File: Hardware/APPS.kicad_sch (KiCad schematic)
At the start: 20 parts, among them SW1 SW_Push, U1 STM32L4P5RET6, Y1 Crystal 8 MHz

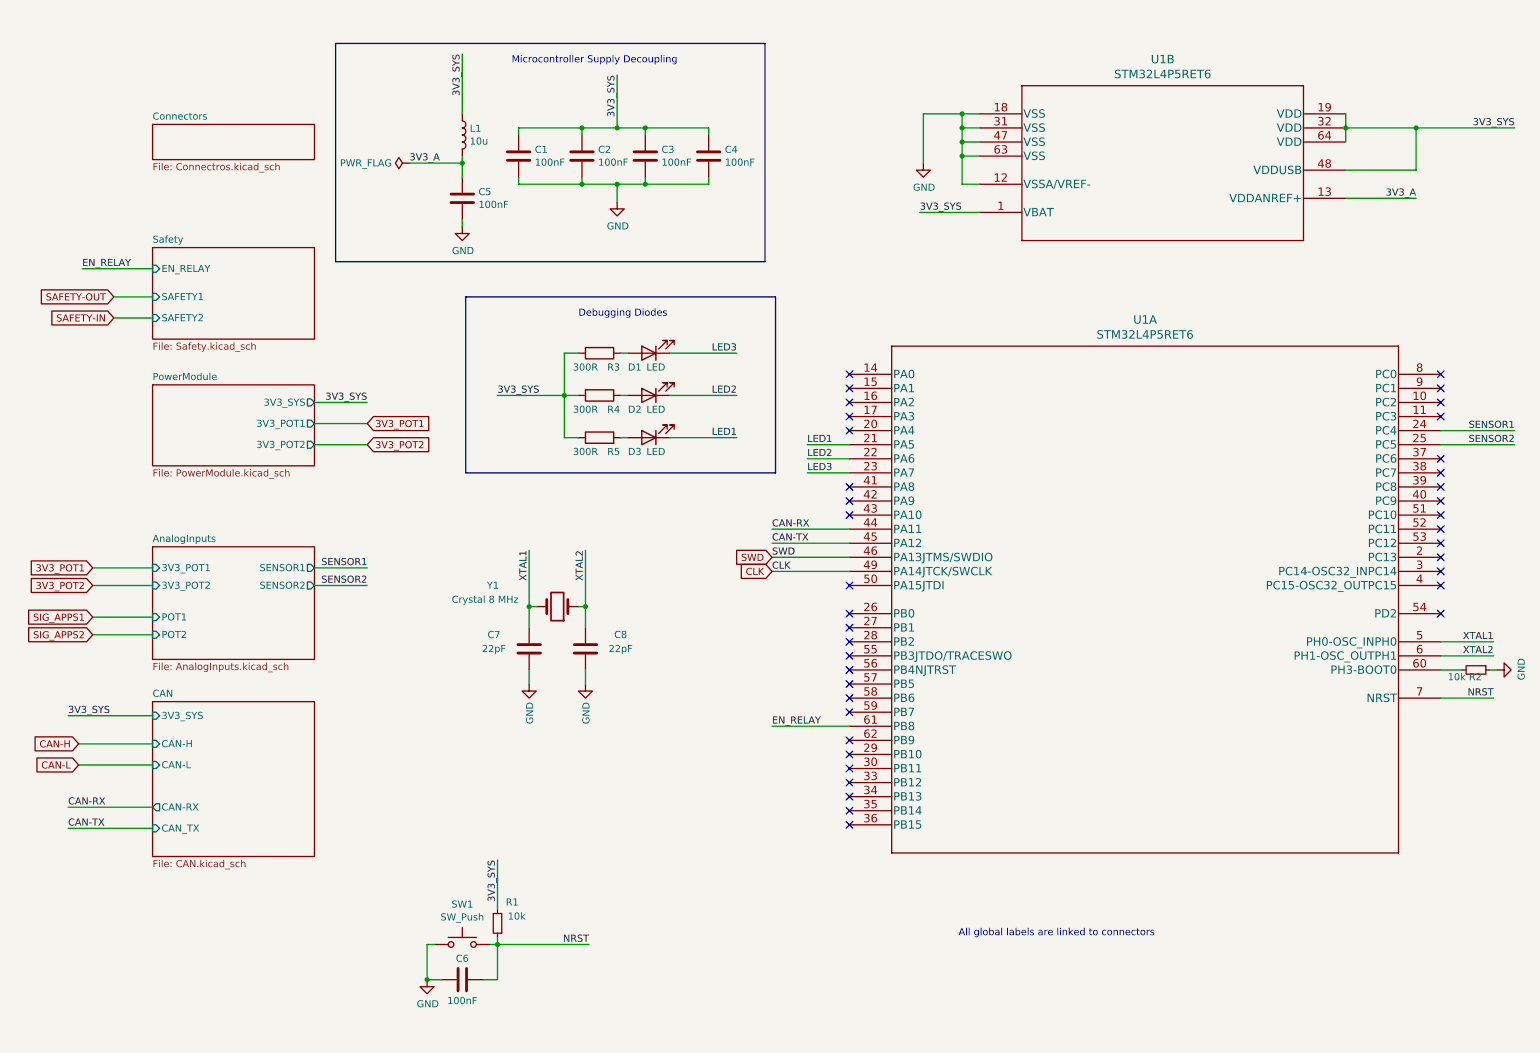
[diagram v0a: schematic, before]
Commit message: Schematic cleanup and description
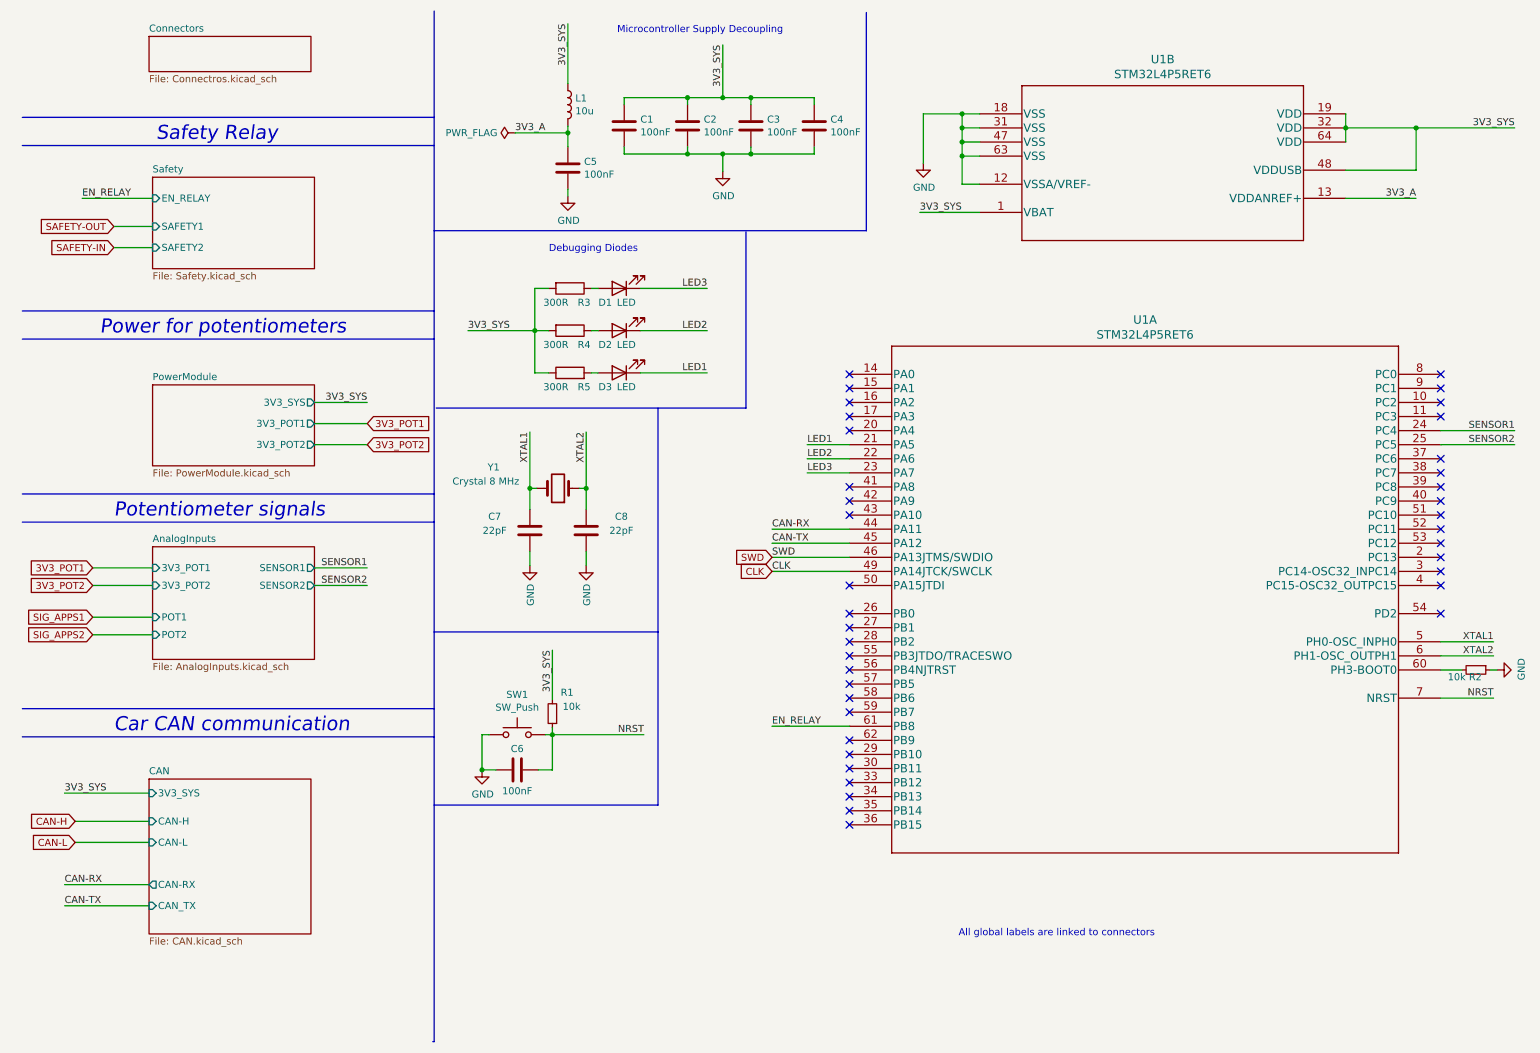
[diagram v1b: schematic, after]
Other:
- note added: "Car CAN communication"
- note added: "Potentiometer signals"
- note added: "Power for potentiometers"
- note added: "Safety Relay"
- moved on the sheet: C1, C2, C3, C4, C5, C6, C7, C8, D1, D2, D3, L1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

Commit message: PCB layout and routing
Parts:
- C5: footprint Capacitor_SMD:C_1206_3216Metric -> Capacitor_SMD:C_0603_1608Metric_Pad1.08x0.95mm_HandSolder
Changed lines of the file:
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@@
       (effects (font (size 1.27 1.27)) (justify left))
     )
-    (property "Footprint" "Capacitor_SMD:C_1206_3216Metric" (id 2) (at 111.4552 44.069 0)
+    (property "Footprint" "Capacitor_SMD:C_0603_1608Metric_Pad1.08x0.95mm_HandSolder" (id 2) (at 111.4552 44.069 0)
       (effects (font (size 1.27 1.27)) hide)
     )
@@
       (reference "#PWR0110") (unit 1) (value "GND") (footprint "")
     )
-    (path "/00000000-0000-0000-0000-00006077b773/97b42d25-e8ef-4cce-8b23-9b6436401edc"
+    (path "/00000000-0000-0000-0000-00006077b773/19768f2f-1e95-477c-97b8-06e4b42f3896"
       (reference "#PWR0111") (unit 1) (value "+24V") (footprint "")
     )
@@
     )
     (path "/00000000-0000-0000-0000-00005f621186"
-      (reference "C5") (unit 1) (value "100nF") (footprint "Capacitor_SMD:C_1206_3216Metric")
+      (reference "C5") (unit 1) (value "100nF") (footprint "Capacitor_SMD:C_0603_1608Metric_Pad1.08x0.95mm_HandSolder")
     )
     (path "/00000000-0000-0000-0000-00005f62a6cf"

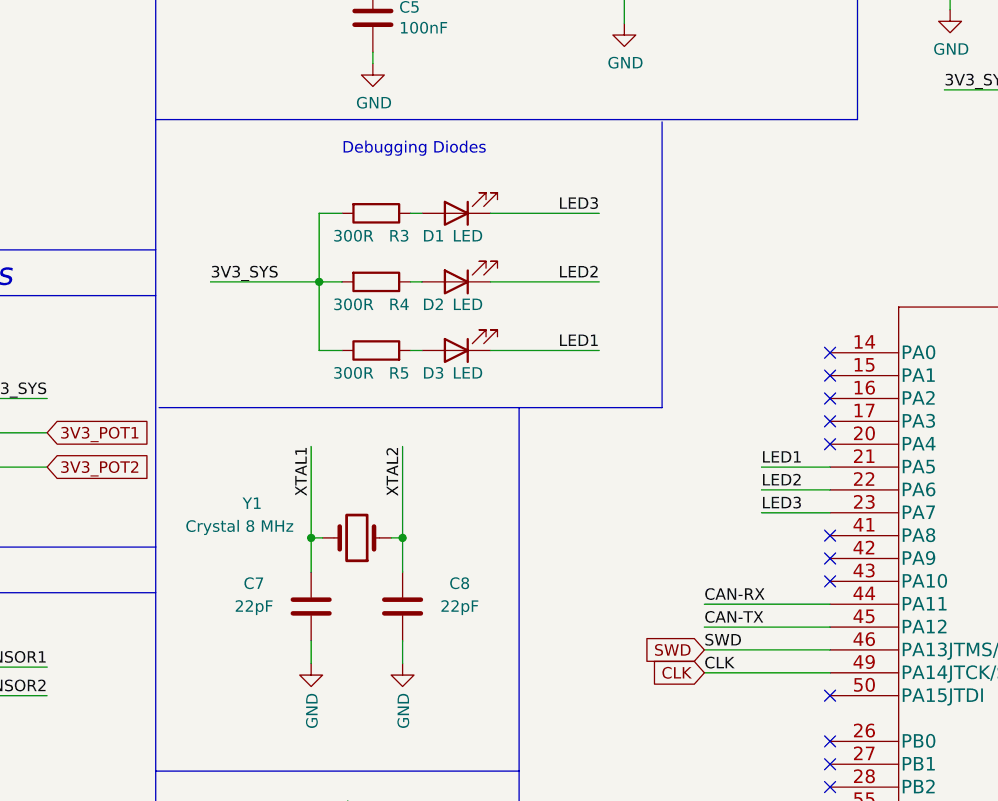
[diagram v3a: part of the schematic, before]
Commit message: Changed crystal footprint, fixed capactiors, added debug LED
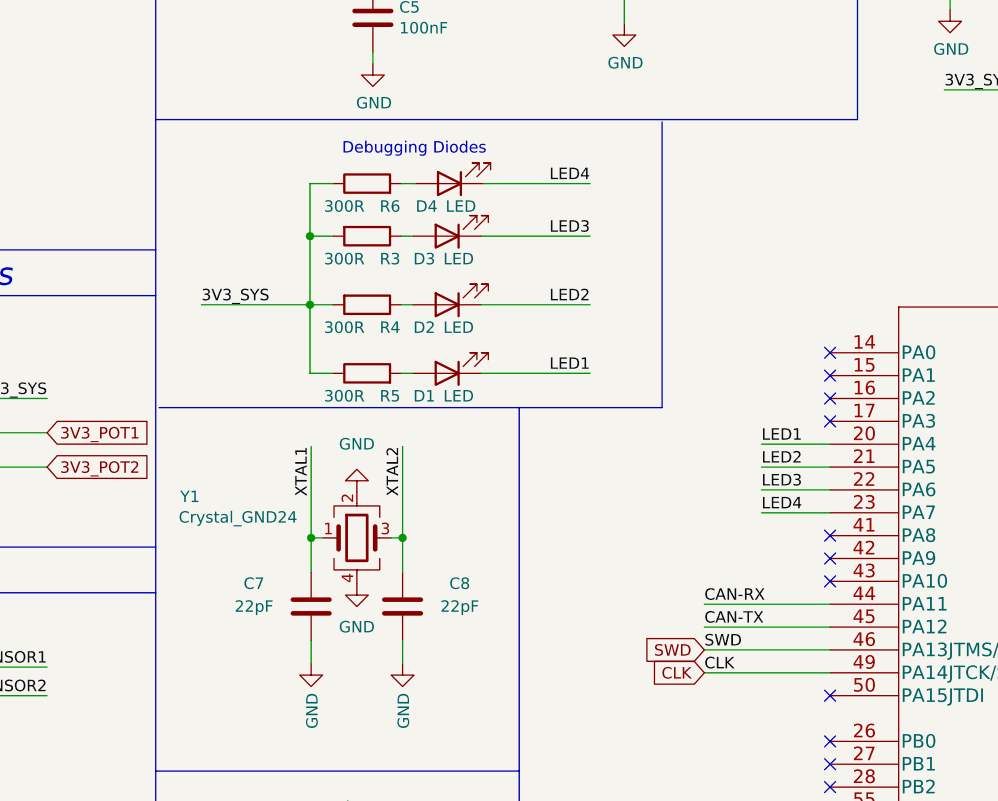
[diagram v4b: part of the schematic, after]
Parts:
- removed Y1: Crystal 8 MHz, Crystal:Crystal_SMD_HC49-SD, symbol Device:Crystal
- added D4: LED, LED_SMD:LED_0603_1608Metric_Pad1.05x0.95mm_HandSolder, symbol Device:LED
- added R6: 300R, Resistor_SMD:R_0603_1608Metric_Pad0.98x0.95mm_HandSolder, symbol Device:R
- added Y1: Crystal_GND24, Crystal:Crystal_SMD_2520-4Pin_2.5x2.0mm, symbol Device:Crystal_GND24
- U1: footprint footprints:STM32L4P5RET6 -> LQFP-64
- U1: footprint footprints:STM32L4P5RET6 -> Package_QFP:LQFP-64_10x10mm_P0.5mm
- renumbered D3 to D1, D1 to D3
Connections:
- net 3V3_SYS: now also R6.1
- net GND: now also Y1.2, Y1.4
- net LED1: now also U1.20 (PA4); no longer U1.21 (PA5)
- net LED2: now also U1.21 (PA5); no longer U1.22 (PA6)
- net LED3: now also U1.22 (PA6); no longer U1.23 (PA7)
- net XTAL1: now also Y1.1
- net XTAL2: now also Y1.3
- new net: D4.2 (A), R6.2
- new net LED4: D4.1 (K), U1.23 (PA7)
- no-connect marks 39 -> 38
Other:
- moved on the sheet: D1, D2, D3, R3, R4, R5

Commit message: Schematic cleanup
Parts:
- removed unit 2 of U1
- U1: footprint LQFP-64 -> Package_QFP:LQFP-64_10x10mm_P0.5mm; symbol 2021-05-10_08-39-16:STM32L4P5RET6 -> STM32L4P5RET6:STM32L4P5RET6
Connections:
- net 3V3_A: now also U1.13 (VDDA/VREF+)
- net 3V3_SYS: now also U1.1 (VBAT), U1.19 (VDD), U1.32 (VDD), U1.48 (VDDUSB), U1.64 (VDD)
- net GND: now also U1.12 (VSSA/VREF-), U1.18 (VSS), U1.31 (VSS), U1.47 (VSS), U1.63 (VSS)
- no-connect marks 38 -> 0
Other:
- note added: "Debug diodes"
- note added: "Oscilator"
- note added: "Reset button"
- note removed: "All global labels are linked to connectors"
- note removed: "Debugging Diodes"
- title: (none) -> PUT Motorsport EV APPS
- moved on the sheet: C1, C2, C3, C4, C5, C6, C7, C8, D1, D2, D3, D4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

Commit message: Generated BOM
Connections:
- no-connect marks 0 -> 38
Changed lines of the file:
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@@
   (junction (at 231.394 141.224) (diameter 0) (color 0 0 0 0)
   )
+  (no_connect (at 249.174 59.436))
+  (no_connect (at 249.174 56.896))
+  (no_connect (at 249.174 54.356))
+  (no_connect (at 249.174 51.816))
+  (no_connect (at 249.174 110.236))
+  (no_connect (at 249.174 112.776))
+  (no_connect (at 249.174 107.696))
+  (no_connect (at 249.174 94.996))
+  (no_connect (at 249.174 97.536))
+  (no_connect (at 249.174 100.076))
+  (no_connect (at 249.174 102.616))
+  (no_connect (at 249.174 105.156))
+  (no_connect (at 249.174 89.916))
+  (no_connect (at 249.174 77.216))
+  (no_connect (at 249.174 74.676))
+  (no_connect (at 249.174 72.136))
+  (no_connect (at 213.614 94.996))
+  (no_connect (at 213.614 92.456))
+  (no_connect (at 213.614 87.376))
+  (no_connect (at 213.614 115.316))
+  (no_connect (at 213.614 117.856))
+  (no_connect (at 213.614 100.076))
+  (no_connect (at 213.614 102.616))
+  (no_connect (at 213.614 105.156))
+  (no_connect (at 213.614 107.696))
+  (no_connect (at 249.174 125.476))
+  (no_connect (at 249.174 128.016))
+  (no_connect (at 249.174 130.556))
+  (no_connect (at 249.174 133.096))
+  (no_connect (at 249.174 122.936))
+  (no_connect (at 249.174 120.396))
+  (no_connect (at 249.174 117.856))
+  (no_connect (at 213.614 133.096))
+  (no_connect (at 213.614 130.556))
+  (no_connect (at 213.614 120.396))
+  (no_connect (at 213.614 122.936))
+  (no_connect (at 213.614 125.476))
+  (no_connect (at 213.614 128.016))
   (wire (pts (xy 263.144 79.756) (xy 249.174 79.756))
     (stroke (width 0) (type default) (color 0 0 0 0))
@@
     (stroke (width 0) (type default) (color 0 0 0 0))
   )
-  (wire (pts (xy 213.614 65.786) (xy 204.089 65.786))
+  (wire (pts (xy 199.136 65.786) (xy 213.614 65.786))
     (stroke (width 0) (type default) (color 0 0 0 0))
   )
@@
     (effects (font (size 1.27 1.27)) (justify right bottom))
   )
-  (label "NRST" (at 204.089 65.786 0)
-    (effects (font (size 1.27 1.27)) (justify left bottom))
-  )
   (label "3V3_SYS" (at 236.474 33.274 270)
     (effects (font (size 1.27 1.27)) (justify right bottom))
@@
   (label "CAN-RX" (at 19.685 169.545 0)
     (effects (font (size 1.27 1.27)) (justify left bottom))
-  )
-  (label "NRST" (at 149.098 172.212 180)
-    (effects (font (size 1.27 1.27)) (justify right bottom))
   )
   (global_label "CLK" (shape input) (at 263.144 87.376 0) (fields_autoplaced)
@@
     )
   )
+  (global_label "NRST" (shape input) (at 199.136 65.786 180) (fields_autoplaced)
+    (effects (font (size 1.27 1.27)) (justify right))
+    (property "Intersheet References" "${INTERSHEET_REFS}" (id 0) (at 192.0342 65.7066 0)
+      (effects (font (size 1.27 1.27)) (justify right) hide)
+    )
+  )
   (global_label "SAFETY-IN" (shape input) (at 28.575 54.61 180) (fields_autoplaced)
     (effects (font (size 1.27 1.27)) (justify right))
@@
     (effects (font (size 1.27 1.27)) (justify left))
     (property "Intersheet References" "${INTERSHEET_REFS}" (id 0) (at 269.3992 84.9154 0)
+      (effects (font (size 1.27 1.27)) (justify left) hide)
+    )
+  )
+  (global_label "NRST" (shape input) (at 149.098 172.212 0) (fields_autoplaced)
+    (effects (font (size 1.27 1.27)) (justify left))
+    (property "Intersheet References" "${INTERSHEET_REFS}" (id 0) (at 156.1998 172.2914 0)
       (effects (font (size 1.27 1.27)) (justify left) hide)
     )
@@
     )
     (path "/00000000-0000-0000-0000-00006077b773/ce8385db-ca62-4bf6-93c6-ac67711339c8"
-      (reference "R11") (unit 1) (value "220R") (footprint "Resistor_SMD:R_1206_3216Metric")
+      (reference "R11") (unit 1) (value "220R") (footprint "Resistor_SMD:R_0603_1608Metric_Pad0.98x0.95mm_HandSolder")
     )
     (path "/00000000-0000-0000-0000-00006068dc5c/00000000-0000-0000-0000-0000606aa78d"
@@
     )
     (path "/00000000-0000-0000-0000-00006077b773/ec62a549-ea11-4f6d-b4c1-112c7a1678a2"
-      (reference "R13") (unit 1) (value "0R") (footprint "Resistor_SMD:R_1206_3216Metric")
+      (reference "R13") (unit 1) (value "0R") (footprint "Resistor_SMD:R_0603_1608Metric_Pad0.98x0.95mm_HandSolder")
     )
     (path "/00000000-0000-0000-0000-00006068dc5c/00000000-0000-0000-0000-0000606aa817"
@@
     )
     (path "/00000000-0000-0000-0000-00006077b773/d2333881-e471-403f-813b-3e8fa945ec03"
-      (reference "R15") (unit 1) (value "0R") (footprint "Resistor_SMD:R_1206_3216Metric")
+      (reference "R15") (unit 1) (value "0R") (footprint "Resistor_SMD:R_0603_1608Metric_Pad0.98x0.95mm_HandSolder")
     )
     (path "/00000000-0000-0000-0000-00006068dc5c/00000000-0000-0000-0000-0000606aa793"
@@
     )
     (path "/00000000-0000-0000-0000-00006077b773/07df8f93-7b84-437f-a326-0ed04fce7f97"
-      (reference "R17") (unit 1) (value "220R") (footprint "Resistor_SMD:R_1206_3216Metric")
+      (reference "R17") (unit 1) (value "220R") (footprint "Resistor_SMD:R_0603_1608Metric_Pad0.98x0.95mm_HandSolder")
     )
     (path "/00000000-0000-0000-0000-00006068dc5c/00000000-0000-0000-0000-0000606aa7ed"
